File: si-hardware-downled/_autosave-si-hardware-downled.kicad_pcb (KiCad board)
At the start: 2 copper layers, 95 x 22.9 mm, 24 parts, among them U1 BP2866D, U2 S4525S

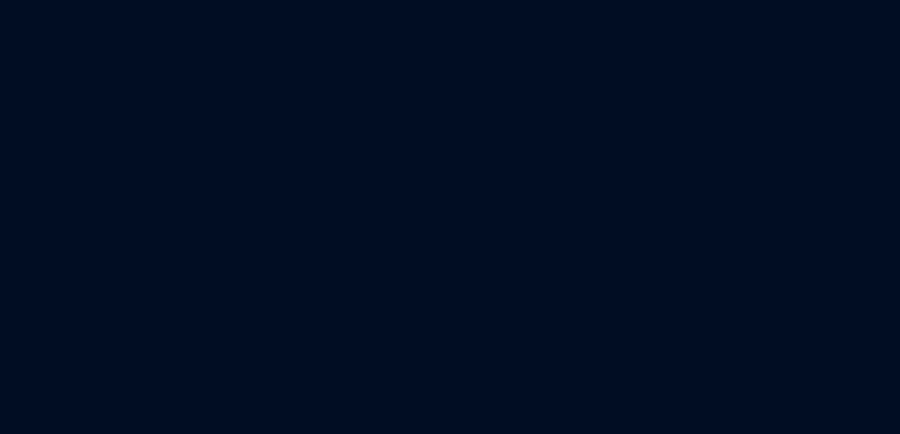
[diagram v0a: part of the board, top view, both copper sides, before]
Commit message: change inductor choke filter
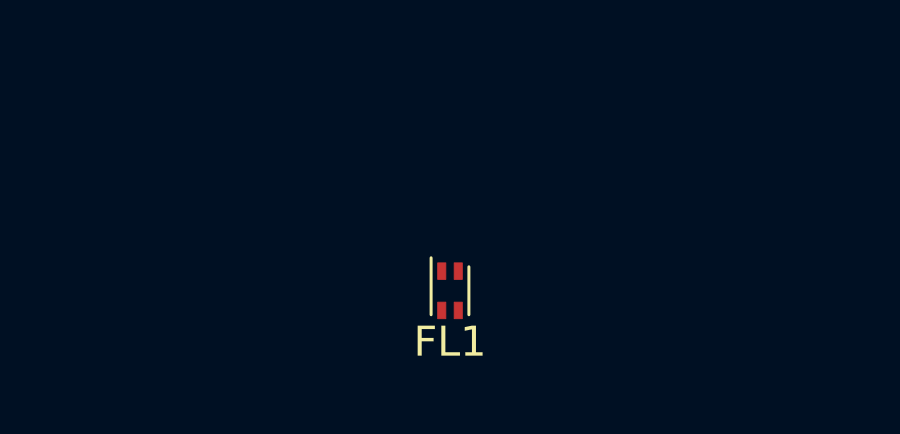
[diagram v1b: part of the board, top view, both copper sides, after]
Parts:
- added FL1: Filter_EMI_LL, Inductor_SMD:L_CommonModeChoke_Coilcraft_0603USB, F.Cu at (162.0, 99.3)
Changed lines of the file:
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@@
 	(net 19 "Net-(J2-Pin_2)")
 	(net 20 "Net-(J2-Pin_3)")
+	(net 21 "VCC1")
 	(footprint ""
 		(layer "F.Cu")
@@
 			(offset
 				(xyz 0 0 0)
+			)
+			(scale
+				(xyz 1 1 1)
+			)
+			(rotate
+				(xyz 0 0 0)
+			)
+		)
+	)
+	(footprint "Inductor_SMD:L_CommonModeChoke_Coilcraft_0603USB"
+		(layer "F.Cu")
+		(at 162.031 99.294)
+		(descr "Coilcraft 0603USB Series Common Mode Choke, https://www.coilcraft.com/pdfs/0603usb.pdf")
+		(tags "surface mount common mode bead")
+		(property "Reference" "FL1"
+			(at 0 1.7 0)
+			(layer "F.SilkS")
+			(effects
+				(font
+					(size 1 1)
+					(thickness 0.15)
+				)
+			)
+		)
+		(property "Value" "Filter_EMI_LL"
+			(at 0 -2.01 0)
+			(layer "F.Fab")
+			(effects
+				(font
+					(size 1 1)
+					(thickness 0.15)
+				)
+			)
+		)
+		(property "Footprint" "Inductor_SMD:L_CommonModeChoke_Coilcraft_0603USB"
+			(at 0 0 0)
+			(unlocked yes)
+			(layer "F.Fab")
+			(hide yes)
+			(effects
+				(font
+					(size 1.27 1.27)
+					(thickness 0.15)
+				)
+			)
+		)
+		(property "Datasheet" ""
+			(at 0 0 0)
+			(unlocked yes)
+			(layer "F.Fab")
+			(hide yes)
+			(effects
+				(font
+					(size 1.27 1.27)
+					(thickness 0.15)
+				)
+			)
+		)
+		(property "Description" "EMI 2-inductor filter"
+			(at 0 0 0)
+			(unlocked yes)
+			(layer "F.Fab")
+			(hide yes)
+			(effects
+				(font
+					(size 1.27 1.27)
+					(thickness 0.15)
+				)
+			)
+		)
+		(property ki_fp_filters "L_* L_CommonMode*")
+		(sheetname "Root")
+		(sheetfile "si-hardware-downled.kicad_sch")
+		(attr smd)
+		(fp_line
+			(start -0.63 -1.1)
+			(end -0.63 0.8)
+			(stroke
+				(width 0.1)
+				(type solid)
+			)
+			(layer "F.SilkS")
+		)
+		(fp_line
+			(start 0.63 0.8)
+			(end 0.63 -0.8)
+			(stroke
+				(width 0.1)
+				(type solid)
+			)
+			(layer "F.SilkS")
+		)
+		(fp_line
+			(start -0.68 -1.2)
+			(end 0.68 -1.2)
+			(stroke
+				(width 0.05)
+				(type solid)
+			)
+			(layer "F.CrtYd")
+		)
+		(fp_line
+			(start -0.68 1.2)
+			(end -0.68 -1.2)
+			(stroke
+				(width 0.05)
+				(type solid)
+			)
+			(layer "F.CrtYd")
+		)
+		(fp_line
+			(start -0.68 1.2)
+			(end 0.68 1.2)
+			(stroke
+				(width 0.05)
+				(type solid)
+			)
+			(layer "F.CrtYd")
+		)
+		(fp_line
+			(start 0.68 1.2)
+			(end 0.68 -1.2)
+			(stroke
+				(width 0.05)
+				(type solid)
+			)
+			(layer "F.CrtYd")
+		)
+		(fp_line
+			(start -0.38 -0.58)
+			(end -0.38 0.76)
+			(stroke
+				(width 0.1)
+				(type solid)
+			)
+			(layer "F.Fab")
+		)
+		(fp_line
+			(start -0.38 -0.58)
+			(end -0.2 -0.76)
+			(stroke
+				(width 0.1)
+				(type solid)
+			)
+			(layer "F.Fab")
+		)
+		(fp_line
+			(start -0.38 0.76)
+			(end 0.38 0.76)
+			(stroke
+				(width 0.1)
+				(type solid)
+			)
+			(layer "F.Fab")
+		)
+		(fp_line
+			(start -0.2 -0.76)
+			(end 0.38 -0.76)
+			(stroke
+				(width 0.1)
+				(type solid)
+			)
+			(layer "F.Fab")
+		)
+		(fp_line
+			(start 0.38 -0.76)
+			(end 0.38 0.76)
+			(stroke
+				(width 0.1)
+				(type solid)
+			)
+			(layer "F.Fab")
+		)
+		(fp_text user "${REFERENCE}"
+			(at 0 0 90)
+			(layer "F.Fab")
+			(effects
+				(font
+					(size 0.5 0.5)
+					(thickness 0.075)
+				)
+			)
+		)
+		(pad "1" smd roundrect
+			(at -0.275 -0.655)
+			(size 0.3 0.58)
+			(layers "F.Cu" "F.Paste" "F.Mask")
+			(roundrect_rratio 0.05)
+			(net 6 "Net-(D2-A)")
+			(pinfunction "1")
+			(pintype "passive")
+		)
+		(pad "2" smd roundrect
+			(at -0.275 0.655)
+			(size 0.3 0.58)
+			(layers "F.Cu" "F.Paste" "F.Mask")
+			(roundrect_rratio 0.05)
+			(net 17 "GND1")
+			(pinfunction "2")
+			(pintype "passive")
+		)
+		(pad "3" smd roundrect
+			(at 0.275 0.655)
+			(size 0.3 0.58)
+			(layers "F.Cu" "F.Paste" "F.Mask")
+			(roundrect_rratio 0.05)
+			(net 5 "VCC")
+			(pinfunction "3")
+			(pintype "passive")
+		)
+		(pad "4" smd roundrect
+			(at 0.275 -0.655)
+			(size 0.3 0.58)
+			(layers "F.Cu" "F.Paste" "F.Mask")
+			(roundrect_rratio 0.05)
+			(net 21 "VCC1")
+			(pinfunction "4")
+			(pintype "passive")
+		)
+		(model "${KICAD8_3DMODEL_DIR}/Inductor_SMD.3dshapes/L_CommonModeChoke_Coilcraft_0603USB.wrl"
+			(offset
+				(xyz 0 0 0)
